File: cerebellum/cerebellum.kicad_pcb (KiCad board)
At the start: 4 copper layers, 95 x 56 mm, 30 parts, among them J1 GPIO, J2 MOTA, J3 MOTB, J4 MD_POW, J5 SPI Conn_SPI, J6 UART Conn_UART, J7 I2C Conn_I2C, J8 VBUS(OUT), J9 3V3(OUT), SW1 SW_PULLUP, SW2 SW_PULLDOWN, U2 POLOLU_TB6612_CARRIER, U3 HC-SR04

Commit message: update footprints
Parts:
- removed J5 SPI: Conn_SPI, Connector_PinHeader_2.54mm:PinHeader_1x04_P2.54mm_Vertical
- removed J6 UART: Conn_UART, Connector_PinHeader_2.54mm:PinHeader_1x02_P2.54mm_Vertical
- removed J7 I2C: Conn_I2C, Connector_PinHeader_2.54mm:PinHeader_1x02_P2.54mm_Vertical
- removed OFF POW ON: on, Button_Switch_THT:SW_E-Switch_EG1271_SPDT
- added J5: Conn_SPI, Connector_PinHeader_2.54mm:PinHeader_1x04_P2.54mm_Vertical, F.Cu at (170.9, 85.5)
- added J6: Conn_UART, Connector_PinHeader_2.54mm:PinHeader_1x02_P2.54mm_Vertical, F.Cu at (175.5, 91.9)
- added J7: Conn_I2C, Connector_PinHeader_2.54mm:PinHeader_1x02_P2.54mm_Vertical, F.Cu at (180.1, 91.9)
- added SW3: SW_SPDT, Button_Switch_THT:SW_E-Switch_EG1271_SPDT, F.Cu at (175.9, 84.8)
- D1: value RKGB -> LED_RKGB; footprint LED_THT:LED_D5.0mm-4_RGB -> LED_THT:LED_D5.0mm-4_RGB_Wide_Pins
- J2: value MOTA -> Conn_MOTA
- J3: value MOTB -> Conn_MOTB
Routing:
- net Net-(D1-RA): track 16.2 -> 0.36 mm
- net Net-(D1-GA): track 12.1 -> 0.11 mm
- net Net-(D1-BA): track 9.20 -> 0.00 mm

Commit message: adjust layout
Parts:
- OFF     ON: renamed from SW3
- moved OFF     ON 68.8 mm to (113.4, 56.0), turned to 180 degrees
- moved J7 54.0 mm to (140.6, 55.1), turned to -90 degrees
- moved J2 44.2 mm to (95.1, 96.0), turned to 180 degrees
- moved J3 43.3 mm to (95.1, 48.0), turned to 0 degrees
- moved J6 39.6 mm to (160.9, 55.1), turned to -90 degrees
- moved J5 35.2 mm to (153.3, 55.1), turned to -90 degrees
- moved D1 15.1 mm to (111.7, 90.3), turned to -90 degrees
- moved R5 13.3 mm to (123.0, 96.8), turned to 90 degrees
- moved R7 11.6 mm to (116.8, 96.8), turned to 90 degrees
- moved R6 11.6 mm to (119.9, 96.8), turned to 90 degrees
- moved J4 11.1 mm to (76.1, 91.2)
- moved G*** 10.3 mm to (77.1, 49.8)
- moved J8 9.65 mm to (160.9, 87.9)
- moved SW2 6.61 mm to (141.8, 90.5), turned to -90 degrees
- moved SW1 5.98 mm to (132.2, 90.5), turned to -90 degrees
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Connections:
- J4 pad 1: /VMOT -> GND
- J4 pad 2: GND -> /VMOT
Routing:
- net +5V: track 154.6 -> 0.00 mm, vias 3 -> 0
- net PICO3.3: track 115.1 -> 0.00 mm, vias 2 -> 0
- net /TRIG: track 68.7 -> 0.00 mm
- net Net-(U3-ECHO): track 61.9 -> 0.00 mm, vias 2 -> 0
- net /AENC_Y: track 51.9 -> 0.00 mm
- net /BENC_W: track 50.5 -> 0.00 mm
- net /AENC_W: track 49.2 -> 0.00 mm
- net /BENC_Y: track 47.5 -> 0.00 mm
- net /SDA: track 39.5 -> 0.00 mm
- net /R_LED: track 33.1 -> 0.00 mm
- net /STBY: track 32.8 -> 0.00 mm
- net /SCL: track 32.7 -> 0.00 mm
- net /PWMB: track 28.2 -> 0.00 mm
- net /PWMA: track 28.1 -> 0.00 mm
- net /BIN2: track 25.8 -> 0.00 mm
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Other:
- board text removed: "GP0"
- board text removed: "GP15"
- board text removed: "GP16"
- board text removed: "Micro-USB"
- board text removed: "VBUS"

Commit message: update layout
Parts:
- moved J3 47.3 mm to (95.2, 95.2), turned to 180 degrees
- moved J2 40.6 mm to (96.8, 55.4)
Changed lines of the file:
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@@
 	(footprint "Connector_JST:JST_SH_BM06B-SRSS-TB_1x06-1MP_P1.00mm_Vertical"
 		(layer "F.Cu")
-		(at 95.1 96 180)
+		(at 96.825 55.4 180)
 		(descr "JST SH series connector, BM06B-SRSS-TB (http://www.jst-mfg.com/product/pdf/eng/eSH.pdf), generated with kicad-footprint-generator")
 		(tags "connector JST SH vertical")
 		(property "Reference" "J2"
-			(at 0 -3.3 0)
+			(at 0.325 -5.65 90)
 			(layer "F.SilkS")
 			(effects
@@
 	(footprint "Connector_JST:JST_SH_BM06B-SRSS-TB_1x06-1MP_P1.00mm_Vertical"
 		(layer "F.Cu")
-		(at 95.1 48)
+		(at 95.25 95.25 180)
 		(descr "JST SH series connector, BM06B-SRSS-TB (http://www.jst-mfg.com/product/pdf/eng/eSH.pdf), generated with kicad-footprint-generator")
 		(tags "connector JST SH vertical")
@@
 		)
 		(property "Value" "Conn_MOTB"
-			(at -5.93 -0.02 90)
+			(at 0.05 4.5 0)
 			(layer "F.SilkS")
 			(effects
@@
 		(attr smd)
 		(fp_line
-			(start -4.11 -0.04)
-			(end -4.11 1.11)
+			(start 4.11 1.11)
+			(end 3.06 1.11)
 			(stroke
 				(width 0.12)
@@
 		)
 		(fp_line
-			(start -4.11 1.11)
-			(end -3.06 1.11)
+			(start 4.11 -0.04)
+			(end 4.11 1.11)
 			(stroke
 				(width 0.12)
@@
 		)
 		(fp_line
-			(start -3.06 1.11)
-			(end -3.06 2.1)
+			(start -2.94 -2.01)
+			(end 2.94 -2.01)
 			(stroke
 				(width 0.12)
@@
 		)
 		(fp_line
-			(start -2.94 -2.01)
-			(end 2.94 -2.01)
+			(start -3.06 1.11)
+			(end -3.06 2.1)
 			(stroke
 				(width 0.12)
@@
 		)
 		(fp_line
-			(start 4.11 -0.04)
-			(end 4.11 1.11)
+			(start -4.11 1.11)
+			(end -3.06 1.11)
 			(stroke
 				(width 0.12)
@@
 		)
 		(fp_line
-			(start 4.11 1.11)
-			(end 3.06 1.11)
+			(start -4.11 -0.04)
+			(end -4.11 1.11)
 			(stroke
 				(width 0.12)
@@
 		)
 		(fp_line
-			(start -4.9 -2.6)
-			(end -4.9 2.6)
+			(start 4.9 2.6)
+			(end 4.9 -2.6)
 			(stroke
 				(width 0.05)
@@
 		)
 		(fp_line
-			(start -4.9 2.6)
-			(end 4.9 2.6)
+			(start 4.9 -2.6)
+			(end -4.9 -2.6)
 			(stroke
 				(width 0.05)
@@
 		)
 		(fp_line
-			(start 4.9 -2.6)
-			(end -4.9 -2.6)
+			(start -4.9 2.6)
+			(end 4.9 2.6)
 			(stroke
 				(width 0.05)
@@
 		)
 		(fp_line
-			(start 4.9 2.6)
-			(end 4.9 -2.6)
+			(start -4.9 -2.6)
+			(end -4.9 2.6)
 			(stroke
 				(width 0.05)
@@
 		)
 		(fp_line
-			(start -4 -1.9)
+			(start 4 1)
 			(end 4 -1.9)
 			(stroke
@@
 		)
 		(fp_line
-			(start -4 1)
-			(end -4 -1.9)
+			(start -2.5 0.292893)
+			(end -2 1)
 			(stroke
 				(width 0.1)
@@
 		)
 		(fp_line
-			(start -4 1)
-			(end 4 1)
+			(start -3 1)
+			(end -2.5 0.292893)
 			(stroke
 				(width 0.1)
@@
 		)
 		(fp_line
-			(start -3 1)
-			(end -2.5 0.292893)
+			(start -4 1)
+			(end 4 1)
 			(stroke
 				(width 0.1)
@@
 		)
 		(fp_line
-			(start -2.5 0.292893)
-			(end -2 1)
+			(start -4 1)
+			(end -4 -1.9)
 			(stroke
 				(width 0.1)
@@
 		)
 		(fp_line
-			(start 4 1)
+			(start -4 -1.9)
 			(end 4 -1.9)
 			(stroke
@@
 		)
 		(fp_rect
-			(start -2.65 -1.55)
-			(end -2.35 -0.95)
+			(start 2.35 -1.55)
+			(end 2.65 -0.95)
 			(stroke
 				(width 0.1)
@@
 		)
 		(fp_rect
-			(start -1.65 -1.55)
-			(end -1.35 -0.95)
+			(start 1.35 -1.55)
+			(end 1.65 -0.95)
 			(stroke
 				(width 0.1)
@@
 		)
 		(fp_rect
-			(start -0.65 -1.55)
-			(end -0.35 -0.95)
+			(start 0.35 -1.55)
+			(end 0.65 -0.95)
 			(stroke
 				(width 0.1)
@@
 		)
 		(fp_rect
-			(start 0.35 -1.55)
-			(end 0.65 -0.95)
+			(start -0.65 -1.55)
+			(end -0.35 -0.95)
 			(stroke
 				(width 0.1)
@@
 		)
 		(fp_rect
-			(start 1.35 -1.55)
-			(end 1.65 -0.95)
+			(start -1.65 -1.55)
+			(end -1.35 -0.95)
 			(stroke
 				(width 0.1)
@@
 		)
 		(fp_rect
-			(start 2.35 -1.55)
-			(end 2.65 -0.95)
+			(start -2.65 -1.55)
+			(end -2.35 -0.95)
 			(stroke
 				(width 0.1)
@@
 		)
 		(pad "1" smd roundrect
-			(at -2.5 1.325)
+			(at -2.5 1.325 180)
 			(size 0.6 1.55)
 			(layers "F.Cu" "F.Mask" "F.Paste")
@@
 		)
 		(pad "2" smd roundrect
-			(at -1.5 1.325)
+			(at -1.5 1.325 180)
 			(size 0.6 1.55)
 			(layers "F.Cu" "F.Mask" "F.Paste")
@@
 		)
 		(pad "3" smd roundrect
-			(at -0.5 1.325)
+			(at -0.5 1.325 180)
 			(size 0.6 1.55)
 			(layers "F.Cu" "F.Mask" "F.Paste")
@@
 		)
 		(pad "4" smd roundrect
-			(at 0.5 1.325)
+			(at 0.5 1.325 180)
 			(size 0.6 1.55)
 			(layers "F.Cu" "F.Mask" "F.Paste")
@@
 		)
 		(pad "5" smd roundrect
-			(at 1.5 1.325)
+			(at 1.5 1.325 180)
 			(size 0.6 1.55)
 			(layers "F.Cu" "F.Mask" "F.Paste")
@@
 		)
 		(pad "6" smd roundrect
-			(at 2.5 1.325)
+			(at 2.5 1.325 180)
 			(size 0.6 1.55)
 			(layers "F.Cu" "F.Mask" "F.Paste")
@@
 		)
 		(pad "MP" smd roundrect
-			(at -3.8 -1.2)
+			(at -3.8 -1.2 180)
 			(size 1.2 1.8)
 			(layers "F.Cu" "F.Mask" "F.Paste")
@@
 		)
 		(pad "MP" smd roundrect
-			(at 3.8 -1.2)
+			(at 3.8 -1.2 180)
 			(size 1.2 1.8)
 			(layers "F.Cu" "F.Mask" "F.Paste")
@@
 	)
 	(gr_text "K"
-		(at 94.1 93.5 90)
+		(at 94.525 92.675 90)
 		(layer "F.SilkS")
 		(effects
@@
 	)
 	(gr_text "B"
-		(at 95.1 93.5 90)
+		(at 95.525 92.675 90)
 		(layer "F.SilkS")
 		(effects
@@
 	)
 	(gr_text "W"
-		(at 97.1 93.557143 90)
+		(at 97.525 92.732143 90)
 		(layer "F.SilkS")
 		(effects
@@
 	)
 	(gr_text "Y"
-		(at 96.1 93.442857 90)
+		(at 96.525 92.617857 90)
 		(layer "F.SilkS")
 		(effects
@@
 	)
 	(gr_text "G"
-		(at 98.1 93.5 90)
+		(at 98.525 92.675 90)
 		(layer "F.SilkS")
 		(effects
@@
 	)
 	(gr_text "R"
-		(at 93.1 93.5 90)
+		(at 93.525 92.675 90)
 		(layer "F.SilkS")
 		(effects

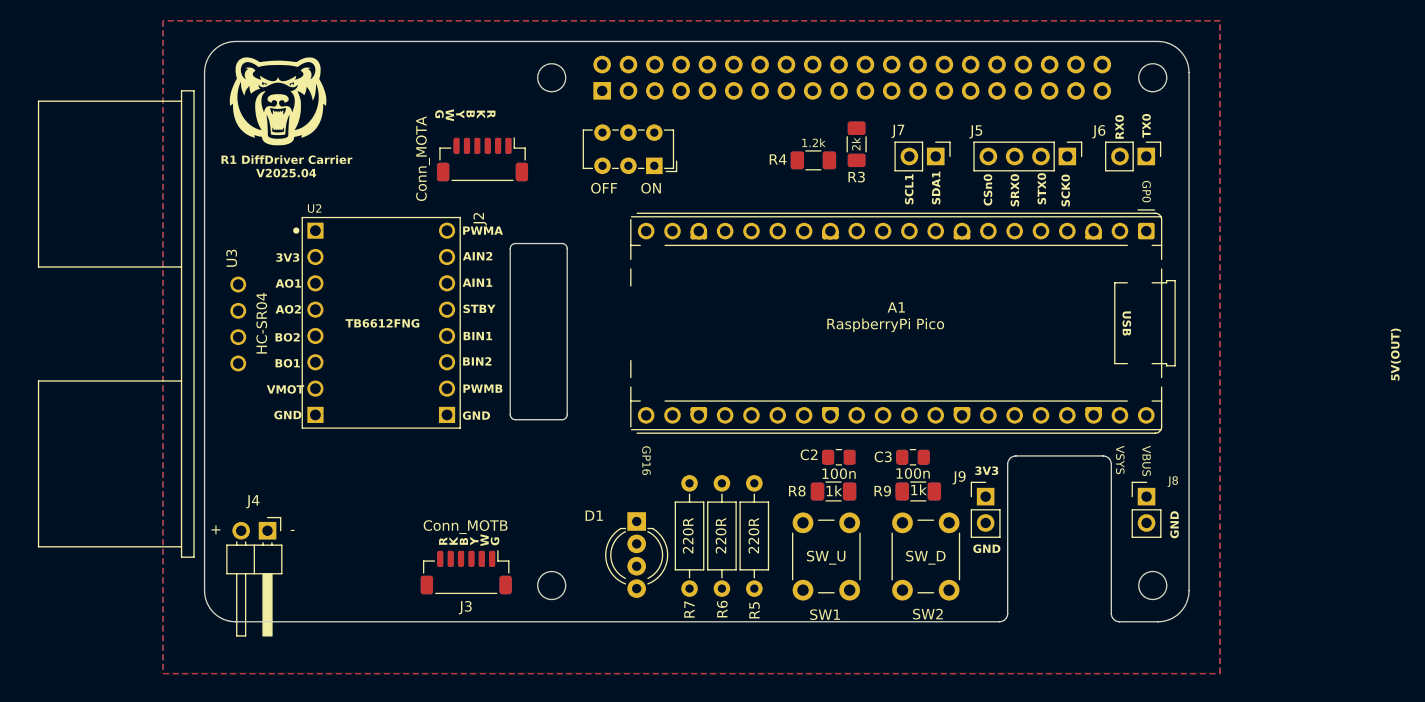
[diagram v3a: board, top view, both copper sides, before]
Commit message: update wiring
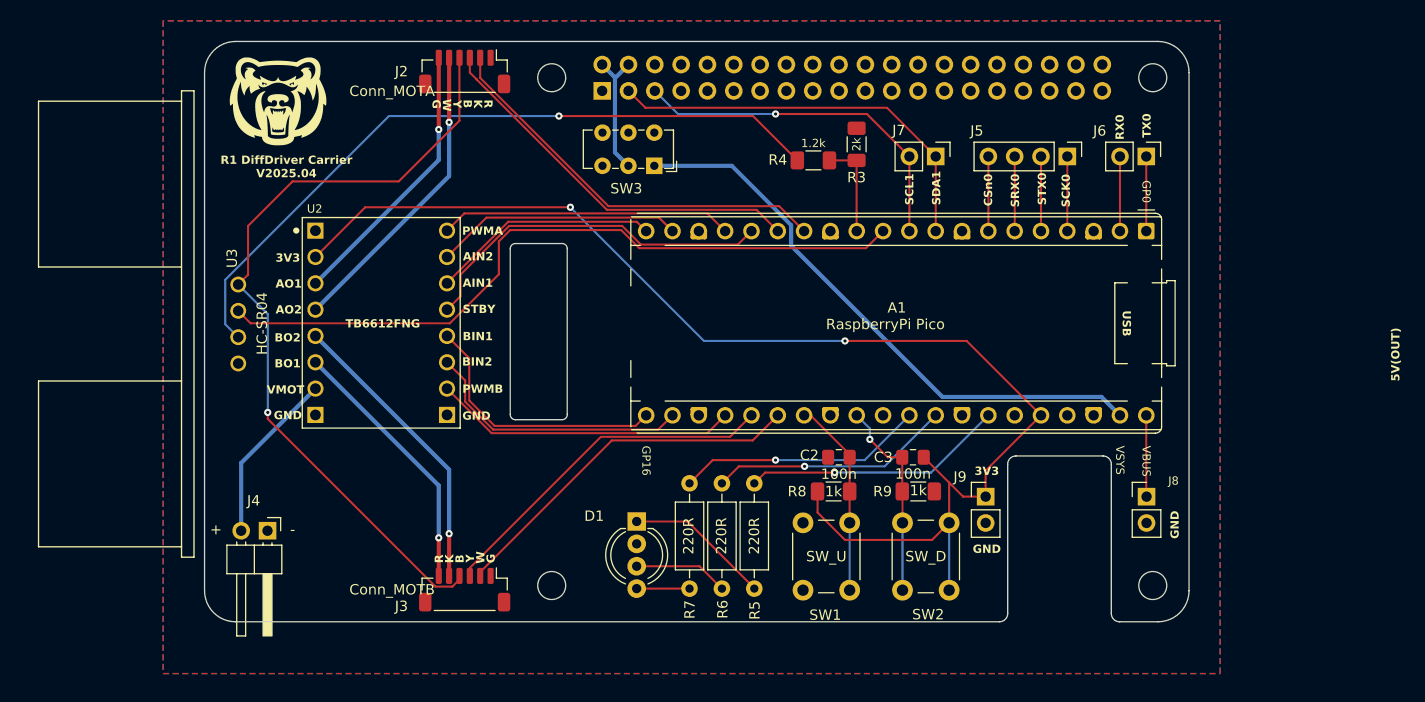
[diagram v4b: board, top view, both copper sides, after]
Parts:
- SW3: renamed from OFF     ON
- moved J2 8.67 mm to (95.1, 46.9)
- moved J3 1.66 mm to (95.1, 96.9)
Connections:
- A1 pad 14: /AENC_Y -> /AENC_W
- A1 pad 15: /AENC_W -> /AENC_Y
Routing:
- net PICO3.3: track 0.00 -> 124.8 mm, vias 0 -> 2
- net +5V: track 0.00 -> 89.4 mm, vias 0 -> 1
- net /TRIG: track 0.00 -> 69.7 mm
- net Net-(U3-ECHO): track 0.00 -> 69.6 mm, vias 0 -> 1
- net VSYS: track 0.00 -> 56.1 mm
- net /SDA: track 0.00 -> 39.5 mm
- net /AENC_W: track 0.00 -> 39.3 mm
- net /AENC_Y: track 0.00 -> 37.5 mm
- net /BENC_W: track 0.00 -> 35.4 mm
- net /STBY: track 0.00 -> 35.2 mm
- net /SCL: track 0.00 -> 34.4 mm, vias 0 -> 1
- net /BENC_Y: track 0.00 -> 34.0 mm
- net /AO2: track 0.00 -> 29.6 mm, vias 0 -> 1
- net /PWMB: track 0.00 -> 29.3 mm
- net /BO2: track 0.00 -> 28.5 mm, vias 0 -> 1
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
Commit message: update design
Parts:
- J2: value Conn_MOTA -> MOTA
- J3: value Conn_MOTB -> MOTB
- SW1: value SW_PULLUP -> PULLUP
- SW2: value SW_PULLDOWN -> PULLDOWN
- SW3: footprint Button_Switch_THT:SW_E-Switch_EG1271_SPDT -> Connector_PinHeader_2.54mm:PinHeader_1x03_P2.54mm_Vertical
- moved SW3 1.18 mm to (113.5, 54.8), turned to -90 degrees
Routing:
- net +5V: track 89.4 -> 103.6 mm, vias 1 -> 2
- net VSYS: track 56.1 -> 56.7 mm
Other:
- board text added: "CerebellumCarrie 25.04"
- board text removed: "R1 DiffDriver Carrier V2025.04"
